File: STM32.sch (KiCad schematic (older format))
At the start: 20 parts, among them U2 STM32F303CBTx

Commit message: added endstops
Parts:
- added C? (x2): 20pF, Capacitors_SMD:C_0603_HandSoldering, symbol Device:C
- added R?: 1M, Resistors_SMD:R_0805_HandSoldering, symbol Device:R
- added Y?: 16MHz, Crystals:Crystal_HC49-4H_Vertical, symbol Device:Crystal
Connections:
- net GND: now also C?.2, C?.2
- new net: C?.1, R?.1, Y?.1
- new net: C?.1, R?.2, Y?.2
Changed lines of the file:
@@
 Text Notes 3450 1900 0    59   ~ 0
 Weak (about 40k ) internal pullup
+$Comp
+L Device:Crystal Y?
+U 1 1 62C7FA0C
+P 1450 3300
+F 0 "Y?" V 1404 3431 50  0000 L CNN
+F 1 "16MHz" V 1495 3431 50  0000 L CNN
+F 2 "Crystals:Crystal_HC49-4H_Vertical" H 1450 3300 50  0001 C CNN
+F 3 "~" H 1450 3300 50  0001 C CNN
+F 4 "Fox Electronics" H 1450 3300 50  0001 C CNN "Manufacturer"
+F 5 "FC4STCBMF16.0-BAG200" H 1450 3300 50  0001 C CNN "Manufacturer P/N"
+F 6 "Digi-Key" H 1450 3300 50  0001 C CNN "Vendor"
+F 7 "631-1108-ND" H 1450 3300 50  0001 C CNN "Vendor P/N"
+	1    1450 3300
+	0    1    1    0
+$EndComp
+Wire Wire Line
+	1250 3050 1450 3050
+Wire Wire Line
+	1450 3150 1450 3050
+Wire Wire Line
+	1450 3450 1450 3600
+$Comp
+L power:GND #PWR?
+U 1 1 62C7FA15
+P 700 3700
+F 0 "#PWR?" H 700 3450 50  0001 C CNN
+F 1 "GND" H 705 3527 50  0000 C CNN
+F 2 "" H 700 3700 50  0001 C CNN
+F 3 "" H 700 3700 50  0001 C CNN
+	1    700  3700
+	1    0    0    -1
+$EndComp
+Wire Wire Line
+	700  3700 700  3600
+Wire Wire Line
+	700  3050 950  3050
+Connection ~ 700  3600
+Wire Wire Line
+	700  3600 700  3050
+$Comp
+L Device:C C?
+U 1 1 62C7FA23
+P 1100 3050
+F 0 "C?" V 848 3050 50  0000 C CNN
+F 1 "20pF" V 939 3050 50  0000 C CNN
+F 2 "Capacitors_SMD:C_0603_HandSoldering" H 1138 2900 50  0001 C CNN
+F 3 "~" H 1100 3050 50  0001 C CNN
+F 4 "KEMET" H 1100 3050 50  0001 C CNN "Manufacturer"
+F 5 "C0805C200G5GAC7800" H 1100 3050 50  0001 C CNN "Manufacturer P/N"
+F 6 "Digi-Key" H 1100 3050 50  0001 C CNN "Vendor"
+F 7 "399-C0805C200G5GAC7800CT-ND" H 1100 3050 50  0001 C CNN "Vendor P/N"
+	1    1100 3050
+	0    1    1    0
+$EndComp
+Wire Wire Line
+	700  3600 1000 3600
+Wire Wire Line
+	1300 3600 1450 3600
+$Comp
+L Device:R R?
+U 1 1 62C7FA2E
+P 1900 3300
+F 0 "R?" H 1970 3346 50  0000 L CNN
+F 1 "1M" H 1970 3255 50  0000 L CNN
+F 2 "Resistors_SMD:R_0805_HandSoldering" V 1830 3300 50  0001 C CNN
+F 3 "~" H 1900 3300 50  0001 C CNN
+F 4 "Vishay Dale" H 1900 3300 50  0001 C CNN "Manufacturer"
+F 5 "RCS08051M00FKEA" H 1900 3300 50  0001 C CNN "Manufacturer P/N"
+F 6 "541-2853-1-ND" H 1900 3300 50  0001 C CNN "Vendor P/N"
+	1    1900 3300
+	1    0    0    -1
+$EndComp
+Connection ~ 1450 3050
+Connection ~ 1450 3600
+Wire Wire Line
+	1450 3600 1900 3600
+Wire Wire Line
+	1450 3050 1900 3050
+Wire Wire Line
+	1900 3150 1900 3050
+Connection ~ 1900 3050
+Wire Wire Line
+	1900 3050 2150 3050
+Wire Wire Line
+	1900 3450 1900 3600
+Connection ~ 1900 3600
+Wire Wire Line
+	1900 3600 2150 3600
+$Comp
+L Device:C C?
+U 1 1 62C7FA42
+P 1150 3600
+F 0 "C?" V 898 3600 50  0000 C CNN
+F 1 "20pF" V 989 3600 50  0000 C CNN
+F 2 "Capacitors_SMD:C_0603_HandSoldering" H 1188 3450 50  0001 C CNN
+F 3 "~" H 1150 3600 50  0001 C CNN
+F 4 "KEMET" H 1150 3600 50  0001 C CNN "Manufacturer"
+F 5 "C0805C200G5GAC7800" H 1150 3600 50  0001 C CNN "Manufacturer P/N"
+F 6 "Digi-Key" H 1150 3600 50  0001 C CNN "Vendor"
+F 7 "399-C0805C200G5GAC7800CT-ND" H 1150 3600 50  0001 C CNN "Vendor P/N"
+	1    1150 3600
+	0    1    1    0
+$EndComp
 $EndSCHEMATC

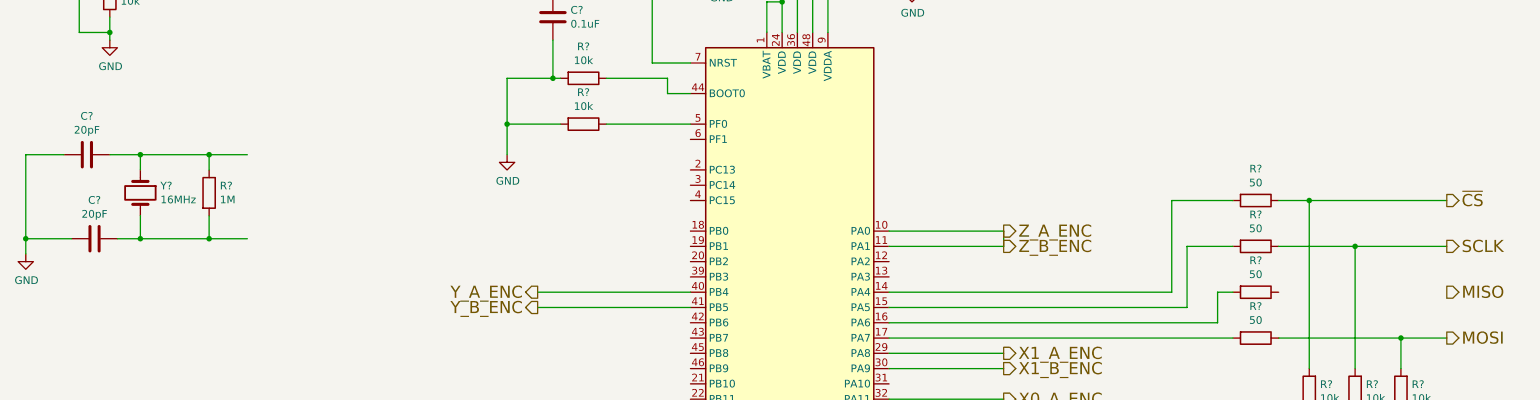
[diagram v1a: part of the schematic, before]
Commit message: removed osc from CoP. added signals to atmega
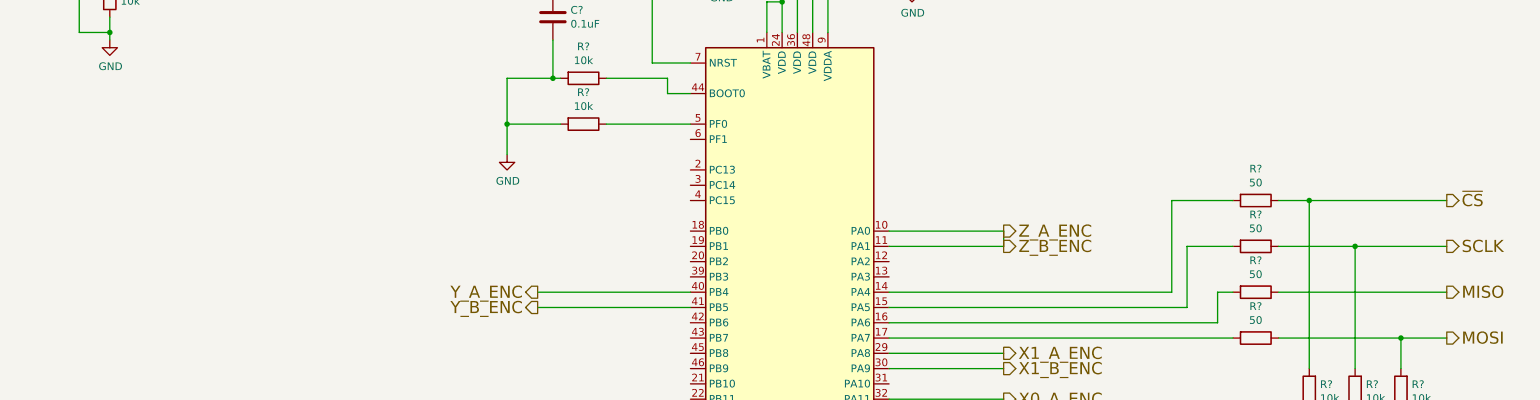
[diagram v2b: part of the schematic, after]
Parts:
- removed C? (x2): 20pF, Capacitors_SMD:C_0603_HandSoldering, symbol Device:C
- removed R?: 1M, Resistors_SMD:R_0805_HandSoldering, symbol Device:R
- removed Y?: 16MHz, Crystals:Crystal_HC49-4H_Vertical, symbol Device:Crystal
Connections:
- net MISO: now also R?.1
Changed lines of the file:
@@
 Text Notes 3450 1900 0    59   ~ 0
 Weak (about 40k ) internal pullup
-$Comp
-L Device:Crystal Y?
-U 1 1 62C7FA0C
-P 1450 3300
-F 0 "Y?" V 1404 3431 50  0000 L CNN
-F 1 "16MHz" V 1495 3431 50  0000 L CNN
-F 2 "Crystals:Crystal_HC49-4H_Vertical" H 1450 3300 50  0001 C CNN
-F 3 "~" H 1450 3300 50  0001 C CNN
-F 4 "Fox Electronics" H 1450 3300 50  0001 C CNN "Manufacturer"
-F 5 "FC4STCBMF16.0-BAG200" H 1450 3300 50  0001 C CNN "Manufacturer P/N"
-F 6 "Digi-Key" H 1450 3300 50  0001 C CNN "Vendor"
-F 7 "631-1108-ND" H 1450 3300 50  0001 C CNN "Vendor P/N"
-	1    1450 3300
-	0    1    1    0
-$EndComp
 Wire Wire Line
-	1250 3050 1450 3050
-Wire Wire Line
-	1450 3150 1450 3050
-Wire Wire Line
-	1450 3450 1450 3600
-$Comp
-L power:GND #PWR?
-U 1 1 62C7FA15
-P 700 3700
-F 0 "#PWR?" H 700 3450 50  0001 C CNN
-F 1 "GND" H 705 3527 50  0000 C CNN
-F 2 "" H 700 3700 50  0001 C CNN
-F 3 "" H 700 3700 50  0001 C CNN
-	1    700  3700
-	1    0    0    -1
-$EndComp
-Wire Wire Line
-	700  3700 700  3600
-Wire Wire Line
-	700  3050 950  3050
-Connection ~ 700  3600
-Wire Wire Line
-	700  3600 700  3050
-$Comp
-L Device:C C?
-U 1 1 62C7FA23
-P 1100 3050
-F 0 "C?" V 848 3050 50  0000 C CNN
-F 1 "20pF" V 939 3050 50  0000 C CNN
-F 2 "Capacitors_SMD:C_0603_HandSoldering" H 1138 2900 50  0001 C CNN
-F 3 "~" H 1100 3050 50  0001 C CNN
-F 4 "KEMET" H 1100 3050 50  0001 C CNN "Manufacturer"
-F 5 "C0805C200G5GAC7800" H 1100 3050 50  0001 C CNN "Manufacturer P/N"
-F 6 "Digi-Key" H 1100 3050 50  0001 C CNN "Vendor"
-F 7 "399-C0805C200G5GAC7800CT-ND" H 1100 3050 50  0001 C CNN "Vendor P/N"
-	1    1100 3050
-	0    1    1    0
-$EndComp
-Wire Wire Line
-	700  3600 1000 3600
-Wire Wire Line
-	1300 3600 1450 3600
-$Comp
-L Device:R R?
-U 1 1 62C7FA2E
-P 1900 3300
-F 0 "R?" H 1970 3346 50  0000 L CNN
-F 1 "1M" H 1970 3255 50  0000 L CNN
-F 2 "Resistors_SMD:R_0805_HandSoldering" V 1830 3300 50  0001 C CNN
-F 3 "~" H 1900 3300 50  0001 C CNN
-F 4 "Vishay Dale" H 1900 3300 50  0001 C CNN "Manufacturer"
-F 5 "RCS08051M00FKEA" H 1900 3300 50  0001 C CNN "Manufacturer P/N"
-F 6 "541-2853-1-ND" H 1900 3300 50  0001 C CNN "Vendor P/N"
-	1    1900 3300
-	1    0    0    -1
-$EndComp
-Connection ~ 1450 3050
-Connection ~ 1450 3600
-Wire Wire Line
-	1450 3600 1900 3600
-Wire Wire Line
-	1450 3050 1900 3050
-Wire Wire Line
-	1900 3150 1900 3050
-Connection ~ 1900 3050
-Wire Wire Line
-	1900 3050 2150 3050
-Wire Wire Line
-	1900 3450 1900 3600
-Connection ~ 1900 3600
-Wire Wire Line
-	1900 3600 2150 3600
-$Comp
-L Device:C C?
-U 1 1 62C7FA42
-P 1150 3600
-F 0 "C?" V 898 3600 50  0000 C CNN
-F 1 "20pF" V 989 3600 50  0000 C CNN
-F 2 "Capacitors_SMD:C_0603_HandSoldering" H 1188 3450 50  0001 C CNN
-F 3 "~" H 1150 3600 50  0001 C CNN
-F 4 "KEMET" H 1150 3600 50  0001 C CNN "Manufacturer"
-F 5 "C0805C200G5GAC7800" H 1150 3600 50  0001 C CNN "Manufacturer P/N"
-F 6 "Digi-Key" H 1150 3600 50  0001 C CNN "Vendor"
-F 7 "399-C0805C200G5GAC7800CT-ND" H 1150 3600 50  0001 C CNN "Vendor P/N"
-	1    1150 3600
-	0    1    1    0
-$EndComp
+	10000 3950 8900 3950
 $EndSCHEMATC

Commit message: connected CoP + mP SPI. pushed updated into layout
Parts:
- gave numbers to parts that had none: 19
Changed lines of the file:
@@
 P 5250 1850
 AR Path="/5EE66603/62277BAE" Ref="#PWR?"  Part="1"
-AR Path="/5EE7212D/62277BAE" Ref="#PWR?"  Part="1"
-F 0 "#PWR?" H 5250 1600 50  0001 C CNN
+AR Path="/5EE7212D/62277BAE" Ref="#PWR0215"  Part="1"
+F 0 "#PWR0215" H 5250 1600 50  0001 C CNN
 F 1 "GND" H 5255 1677 50  0000 C CNN
 F 2 "" H 5250 1850 50  0001 C CNN
@@
 P 4500 1500
 AR Path="/5EE66603/62279669" Ref="C?"  Part="1"
-AR Path="/5EE7212D/62279669" Ref="C?"  Part="1"
-F 0 "C?" H 4615 1546 50  0000 L CNN
+AR Path="/5EE7212D/62279669" Ref="C77"  Part="1"
+F 0 "C77" H 4615 1546 50  0000 L CNN
 F 1 ".1uF" H 4615 1455 50  0000 L CNN
 F 2 "Resistor_SMD:R_0805_2012Metric_Pad1.15x1.40mm_HandSolder" H 4538 1350 50  0001 C CNN
@@
 	4500 1250 4500 1350
 $Comp
-L Device:R R?
+L Device:R R20
 U 1 1 6227B935
 P 6500 1200
-F 0 "R?" H 6570 1246 50  0000 L CNN
+F 0 "R20" H 6570 1246 50  0000 L CNN
 F 1 "R" H 6570 1155 50  0000 L CNN
 F 2 "" V 6430 1200 50  0001 C CNN
@@
 P 6500 1600
 AR Path="/5EE66603/6227D077" Ref="C?"  Part="1"
-AR Path="/5EE7212D/6227D077" Ref="C?"  Part="1"
-F 0 "C?" H 6615 1646 50  0000 L CNN
+AR Path="/5EE7212D/6227D077" Ref="C80"  Part="1"
+F 0 "C80" H 6615 1646 50  0000 L CNN
 F 1 "0.1uF" H 6615 1555 50  0000 L CNN
 F 2 "Capacitor_SMD:C_0603_1608Metric_Pad1.05x0.95mm_HandSolder" H 6538 1450 50  0001 C CNN
@@
 P 6500 1950
 AR Path="/5EE66603/6227D07D" Ref="#PWR?"  Part="1"
-AR Path="/5EE7212D/6227D07D" Ref="#PWR?"  Part="1"
-F 0 "#PWR?" H 6500 1700 50  0001 C CNN
+AR Path="/5EE7212D/6227D07D" Ref="#PWR0216"  Part="1"
+F 0 "#PWR0216" H 6500 1700 50  0001 C CNN
 F 1 "GND" H 6505 1777 50  0000 C CNN
 F 2 "" H 6500 1950 50  0001 C CNN
@@
 P 5850 5750
 AR Path="/5EE66603/622818A4" Ref="#PWR?"  Part="1"
-AR Path="/5EE7212D/622818A4" Ref="#PWR?"  Part="1"
-F 0 "#PWR?" H 5850 5500 50  0001 C CNN
+AR Path="/5EE7212D/622818A4" Ref="#PWR0217"  Part="1"
+F 0 "#PWR0217" H 5850 5500 50  0001 C CNN
 F 1 "GND" H 5855 5577 50  0000 C CNN
 F 2 "" H 5850 5750 50  0001 C CNN
@@
 SWDCLK
 $Comp
-L power:+3.3V #PWR?
+L power:+3.3V #PWR0218
 U 1 1 62AABD48
 P 5650 700
-F 0 "#PWR?" H 5650 550 50  0001 C CNN
+F 0 "#PWR0218" H 5650 550 50  0001 C CNN
 F 1 "+3.3V" H 5665 873 50  0000 C CNN
 F 2 "" H 5650 700 50  0001 C CNN
@@
 	6350 4950 7100 4950
 $Comp
-L power:GND #PWR?
+L power:GND #PWR0219
 U 1 1 62AB3BDD
 P 3850 3050
-F 0 "#PWR?" H 3850 2800 50  0001 C CNN
+F 0 "#PWR0219" H 3850 2800 50  0001 C CNN
 F 1 "GND" H 3855 2877 50  0000 C CNN
 F 2 "" H 3850 3050 50  0001 C CNN
@@
 	4800 1950 4150 1950
 $Comp
-L Device:R R?
+L Device:R R22
 U 1 1 62AC2AF1
 P 4350 2550
-F 0 "R?" V 4143 2550 50  0000 C CNN
+F 0 "R22" V 4143 2550 50  0000 C CNN
 F 1 "10k" V 4234 2550 50  0000 C CNN
 F 2 "Resistor_SMD:R_0805_2012Metric_Pad1.15x1.40mm_HandSolder" V 4280 2550 50  0001 C CNN
@@
 $EndComp
 $Comp
-L Device:R R?
+L Device:R R24
 U 1 1 62AC33E9
 P 4350 2850
-F 0 "R?" V 4143 2850 50  0000 C CNN
+F 0 "R24" V 4143 2850 50  0000 C CNN
 F 1 "10k" V 4234 2850 50  0000 C CNN
 F 2 "Resistor_SMD:R_0805_2012Metric_Pad1.15x1.40mm_HandSolder" V 4280 2850 50  0001 C CNN
@@
 MISO
 $Comp
-L Device:R R?
+L Device:R R25
 U 1 1 62AD17E8
 P 8750 3350
-F 0 "R?" V 8543 3350 50  0000 C CNN
+F 0 "R25" V 8543 3350 50  0000 C CNN
 F 1 "50" V 8634 3350 50  0000 C CNN
 F 2 "Resistor_SMD:R_0805_2012Metric_Pad1.15x1.40mm_HandSolder" V 8680 3350 50  0001 C CNN
@@
 	8600 4250 6350 4250
 $Comp
-L Device:R R?
+L Device:R R35
 U 1 1 62ADB7CE
 P 9100 4600
-F 0 "R?" H 9030 4554 50  0000 R CNN
+F 0 "R35" H 9030 4554 50  0000 R CNN
 F 1 "10k" H 9030 4645 50  0000 R CNN
 F 2 "Resistor_SMD:R_0805_2012Metric_Pad1.15x1.40mm_HandSolder" V 9030 4600 50  0001 C CNN
@@
 $EndComp
 $Comp
-L Device:R R?
+L Device:R R37
 U 1 1 62ADD0C2
 P 9400 4600
-F 0 "R?" H 9330 4554 50  0000 R CNN
+F 0 "R37" H 9330 4554 50  0000 R CNN
 F 1 "10k" H 9330 4645 50  0000 R CNN
 F 2 "Resistor_SMD:R_0805_2012Metric_Pad1.15x1.40mm_HandSolder" V 9330 4600 50  0001 C CNN
@@
 $EndComp
 $Comp
-L Device:R R?
+L Device:R R72
 U 1 1 62ADD50C
 P 9700 4600
-F 0 "R?" H 9630 4554 50  0000 R CNN
+F 0 "R72" H 9630 4554 50  0000 R CNN
 F 1 "10k" H 9630 4645 50  0000 R CNN
 F 2 "Resistor_SMD:R_0805_2012Metric_Pad1.15x1.40mm_HandSolder" V 9630 4600 50  0001 C CNN
@@
 P 9250 4850
 AR Path="/5EE66603/62ADD8AE" Ref="#PWR?"  Part="1"
-AR Path="/5EE7212D/62ADD8AE" Ref="#PWR?"  Part="1"
-F 0 "#PWR?" H 9250 4600 50  0001 C CNN
+AR Path="/5EE7212D/62ADD8AE" Ref="#PWR0220"  Part="1"
+F 0 "#PWR0220" H 9250 4600 50  0001 C CNN
 F 1 "GND" H 9255 4677 50  0000 C CNN
 F 2 "" H 9250 4850 50  0001 C CNN
@@
 P 4900 1500
 AR Path="/5EE66603/62AF32D6" Ref="C?"  Part="1"
-AR Path="/5EE7212D/62AF32D6" Ref="C?"  Part="1"
-F 0 "C?" H 5015 1546 50  0000 L CNN
+AR Path="/5EE7212D/62AF32D6" Ref="C78"  Part="1"
+F 0 "C78" H 5015 1546 50  0000 L CNN
 F 1 ".1uF" H 5015 1455 50  0000 L CNN
 F 2 "Resistor_SMD:R_0805_2012Metric_Pad1.15x1.40mm_HandSolder" H 4938 1350 50  0001 C CNN
@@
 P 5300 1500
 AR Path="/5EE66603/62AF949C" Ref="C?"  Part="1"
-AR Path="/5EE7212D/62AF949C" Ref="C?"  Part="1"
-F 0 "C?" H 5415 1546 50  0000 L CNN
+AR Path="/5EE7212D/62AF949C" Ref="C79"  Part="1"
+F 0 "C79" H 5415 1546 50  0000 L CNN
 F 1 ".1uF" H 5415 1455 50  0000 L CNN
 F 2 "Resistor_SMD:R_0805_2012Metric_Pad1.15x1.40mm_HandSolder" H 5338 1350 50  0001 C CNN
@@
 SWDCLK
 $Comp
-L Connector:Conn_01x04_Female J?
+L Connector:Conn_01x04_Female J16
 U 1 1 62B0343A
 P 1850 1500
-F 0 "J?" H 1878 1476 50  0000 L CNN
+F 0 "J16" H 1878 1476 50  0000 L CNN
 F 1 "Conn_01x04_Female" H 1878 1385 50  0000 L CNN
 F 2 "" H 1850 1500 50  0001 C CNN
@@
 	1050 950  1200 950
 $Comp
-L power:+3.3V #PWR?
+L power:+3.3V #PWR0221
 U 1 1 62B0DE33
 P 1200 850
-F 0 "#PWR?" H 1200 700 50  0001 C CNN
+F 0 "#PWR0221" H 1200 700 50  0001 C CNN
 F 1 "+3.3V" H 1215 1023 50  0000 C CNN
 F 2 "" H 1200 850 50  0001 C CNN
@@
 	1250 1700 1250 1850
 $Comp
-L power:GND #PWR?
+L power:GND #PWR0222
 U 1 1 62B1D272
 P 1250 2300
-F 0 "#PWR?" H 1250 2050 50  0001 C CNN
+F 0 "#PWR0222" H 1250 2050 50  0001 C CNN
 F 1 "GND" H 1255 2127 50  0000 C CNN
 F 2 "" H 1250 2300 50  0001 C CNN
@@
 SWDCLK
 $Comp
-L Device:R R?
+L Device:R R29
 U 1 1 62B3A1E5
 P 8750 3650
-F 0 "R?" V 8543 3650 50  0000 C CNN
+F 0 "R29" V 8543 3650 50  0000 C CNN
 F 1 "50" V 8634 3650 50  0000 C CNN
 F 2 "Resistor_SMD:R_0805_2012Metric_Pad1.15x1.40mm_HandSolder" V 8680 3650 50  0001 C CNN
@@
 $EndComp
 $Comp
-L Device:R R?
+L Device:R R30
 U 1 1 62B3A476
 P 8750 3950
-F 0 "R?" V 8543 3950 50  0000 C CNN
+F 0 "R30" V 8543 3950 50  0000 C CNN
 F 1 "50" V 8634 3950 50  0000 C CNN
 F 2 "Resistor_SMD:R_0805_2012Metric_Pad1.15x1.40mm_HandSolder" V 8680 3950 50  0001 C CNN
@@
 $EndComp
 $Comp
-L Device:R R?
+L Device:R R31
 U 1 1 62B3A881
 P 8750 4250
-F 0 "R?" V 8543 4250 50  0000 C CNN
+F 0 "R31" V 8543 4250 50  0000 C CNN
 F 1 "50" V 8634 4250 50  0000 C CNN
 F 2 "Resistor_SMD:R_0805_2012Metric_Pad1.15x1.40mm_HandSolder" V 8680 4250 50  0001 C CNN
@@
 $EndComp
 $Comp
-L Device:R R?
+L Device:R R5
 U 1 1 62B3AE73
 P 1350 1150
-F 0 "R?" H 1280 1104 50  0000 R CNN
+F 0 "R5" H 1280 1104 50  0000 R CNN
 F 1 "10k" H 1280 1195 50  0000 R CNN
 F 2 "Resistor_SMD:R_0805_2012Metric_Pad1.15x1.40mm_HandSolder" V 1280 1150 50  0001 C CNN
@@
 $EndComp
 $Comp
-L Device:R R?
+L Device:R R21
 U 1 1 62B3B3A7
 P 1250 2000
-F 0 "R?" H 1180 1954 50  0000 R CNN
+F 0 "R21" H 1180 1954 50  0000 R CNN
 F 1 "10k" H 1180 2045 50  0000 R CNN
 F 2 "Resistor_SMD:R_0805_2012Metric_Pad1.15x1.40mm_HandSolder" V 1180 2000 50  0001 C CNN
@@
 $EndComp
 $Comp
-L Device:R R?
+L Device:R R3
 U 1 1 62B3BA13
 P 1050 1150
-F 0 "R?" H 980 1104 50  0000 R CNN
+F 0 "R3" H 980 1104 50  0000 R CNN
 F 1 "10k" H 980 1195 50  0000 R CNN
 F 2 "Resistor_SMD:R_0805_2012Metric_Pad1.15x1.40mm_HandSolder" V 980 1150 50  0001 C CNN
@@
 P 4150 2150
 AR Path="/5EE66603/62B3D441" Ref="C?"  Part="1"
-AR Path="/5EE7212D/62B3D441" Ref="C?"  Part="1"
-F 0 "C?" H 4265 2196 50  0000 L CNN
+AR Path="/5EE7212D/62B3D441" Ref="C81"  Part="1"
+F 0 "C81" H 4265 2196 50  0000 L CNN
 F 1 "0.1uF" H 4265 2105 50  0000 L CNN
 F 2 "Capacitor_SMD:C_0603_1608Metric_Pad1.05x0.95mm_HandSolder" H 4188 2000 50  0001 C CNN

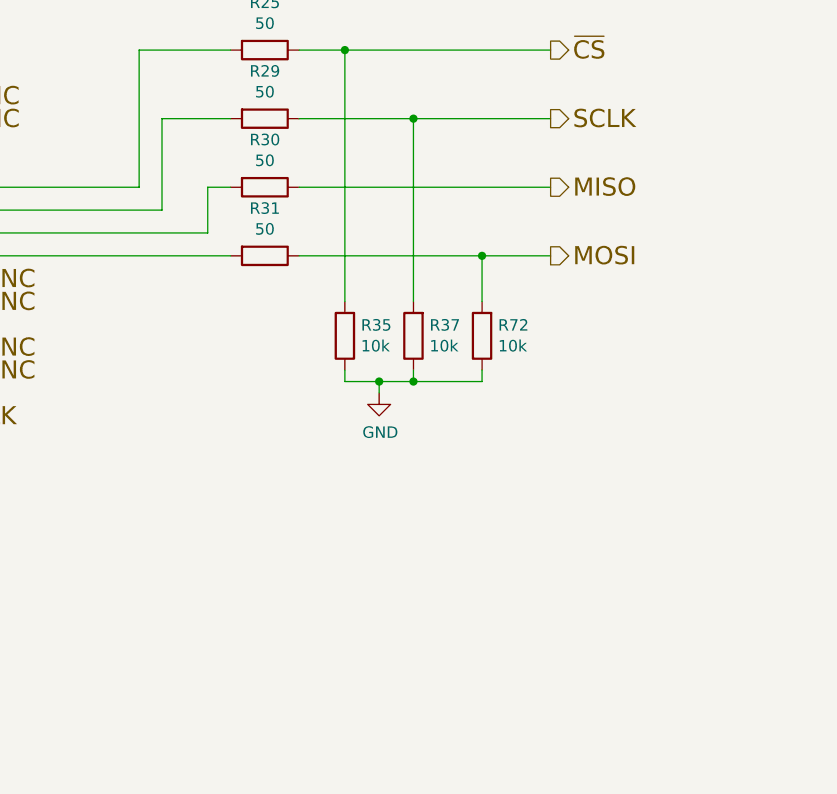
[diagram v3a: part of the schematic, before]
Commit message: added  atmega16. finished CoP. need check VBUS <-> ATMEGA supplies
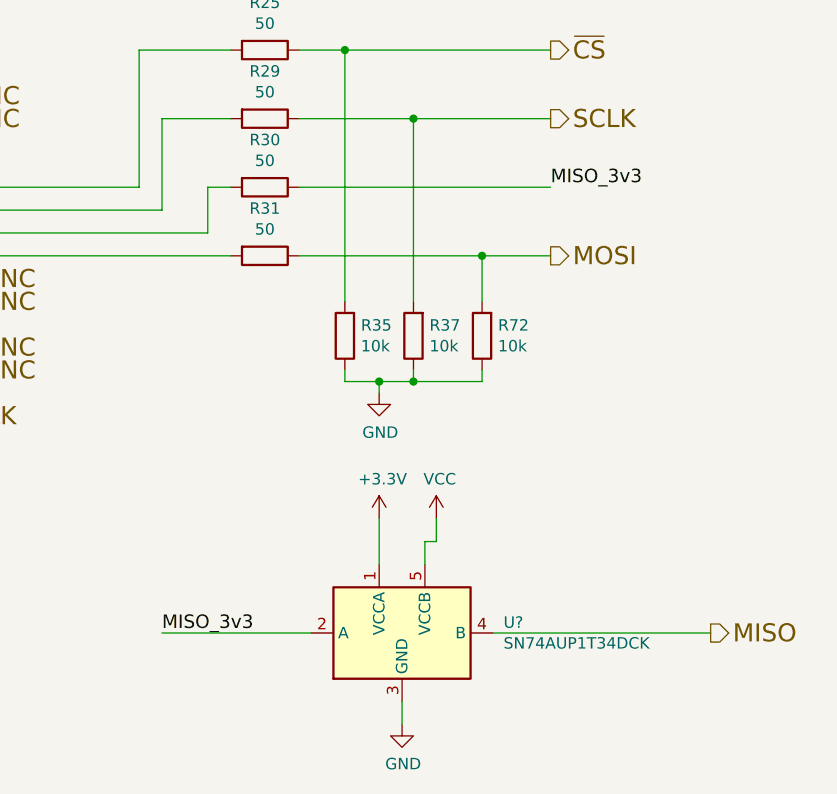
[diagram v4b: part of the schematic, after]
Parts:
- added U?: SN74AUP1T34DCK, Package_TO_SOT_SMD:SOT-353_SC-70-5, symbol Logic_LevelTranslator:SN74AUP1T34DCK
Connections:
- net +3V3: now also U?.1 (VCCA)
- net GND: now also U?.3 (GND)
- net MISO: now also U?.4 (B); no longer R30.1
- new net MISO_3v3: R30.1, U?.2 (A)
- new net VCC: U?.5 (VCCB)
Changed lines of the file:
@@
 $Descr A4 11693 8268
 encoding utf-8
-Sheet 2 8
+Sheet 2 9
 Title ""
 Date ""
@@
 Text HLabel 10000 3650 2    79   Output ~ 0
 SCLK
-Text HLabel 10000 3950 2    79   Output ~ 0
+Text HLabel 10700 5900 2    79   Output ~ 0
 MISO
 $Comp
@@
 Wire Wire Line
 	10000 3950 8900 3950
+$Comp
+L Logic_LevelTranslator:SN74AUP1T34DCK U?
+U 1 1 63165C49
+P 9350 5900
+F 0 "U?" H 9794 5946 50  0000 L CNN
+F 1 "SN74AUP1T34DCK" H 9794 5855 50  0000 L CNN
+F 2 "Package_TO_SOT_SMD:SOT-353_SC-70-5" H 9350 5200 50  0001 C CNN
+F 3 "http://www.ti.com/lit/ds/symlink/sn74aup1t34.pdf" H 9350 5300 50  0001 C CNN
+	1    9350 5900
+	1    0    0    -1
+$EndComp
+Wire Wire Line
+	9750 5900 10700 5900
+Text Label 10000 3950 0    59   ~ 0
+MISO_3v3
+Text Label 8300 5900 0    59   ~ 0
+MISO_3v3
+Wire Wire Line
+	8300 5900 8950 5900
+$Comp
+L power:GND #PWR?
+U 1 1 6316E590
+P 9350 6300
+AR Path="/5EE66603/6316E590" Ref="#PWR?"  Part="1"
+AR Path="/5EE7212D/6316E590" Ref="#PWR?"  Part="1"
+F 0 "#PWR?" H 9350 6050 50  0001 C CNN
+F 1 "GND" H 9355 6127 50  0000 C CNN
+F 2 "" H 9350 6300 50  0001 C CNN
+F 3 "" H 9350 6300 50  0001 C CNN
+	1    9350 6300
+	1    0    0    -1
+$EndComp
+Wire Wire Line
+	9350 6200 9350 6300
+$Comp
+L power:+3.3V #PWR?
+U 1 1 631724AF
+P 9250 5400
+F 0 "#PWR?" H 9250 5250 50  0001 C CNN
+F 1 "+3.3V" H 9265 5573 50  0000 C CNN
+F 2 "" H 9250 5400 50  0001 C CNN
+F 3 "" H 9250 5400 50  0001 C CNN
+	1    9250 5400
+	1    0    0    -1
+$EndComp
+Wire Wire Line
+	9250 5400 9250 5600
+$Comp
+L power:VCC #PWR?
+U 1 1 63188529
+P 9500 5400
+F 0 "#PWR?" H 9500 5250 50  0001 C CNN
+F 1 "VCC" H 9515 5573 50  0000 C CNN
+F 2 "" H 9500 5400 50  0001 C CNN
+F 3 "" H 9500 5400 50  0001 C CNN
+	1    9500 5400
+	1    0    0    -1
+$EndComp
+Wire Wire Line
+	9500 5400 9500 5500
+Wire Wire Line
+	9500 5500 9450 5500
+Wire Wire Line
+	9450 5500 9450 5600
 $EndSCHEMATC
